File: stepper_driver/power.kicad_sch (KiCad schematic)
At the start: 3 parts

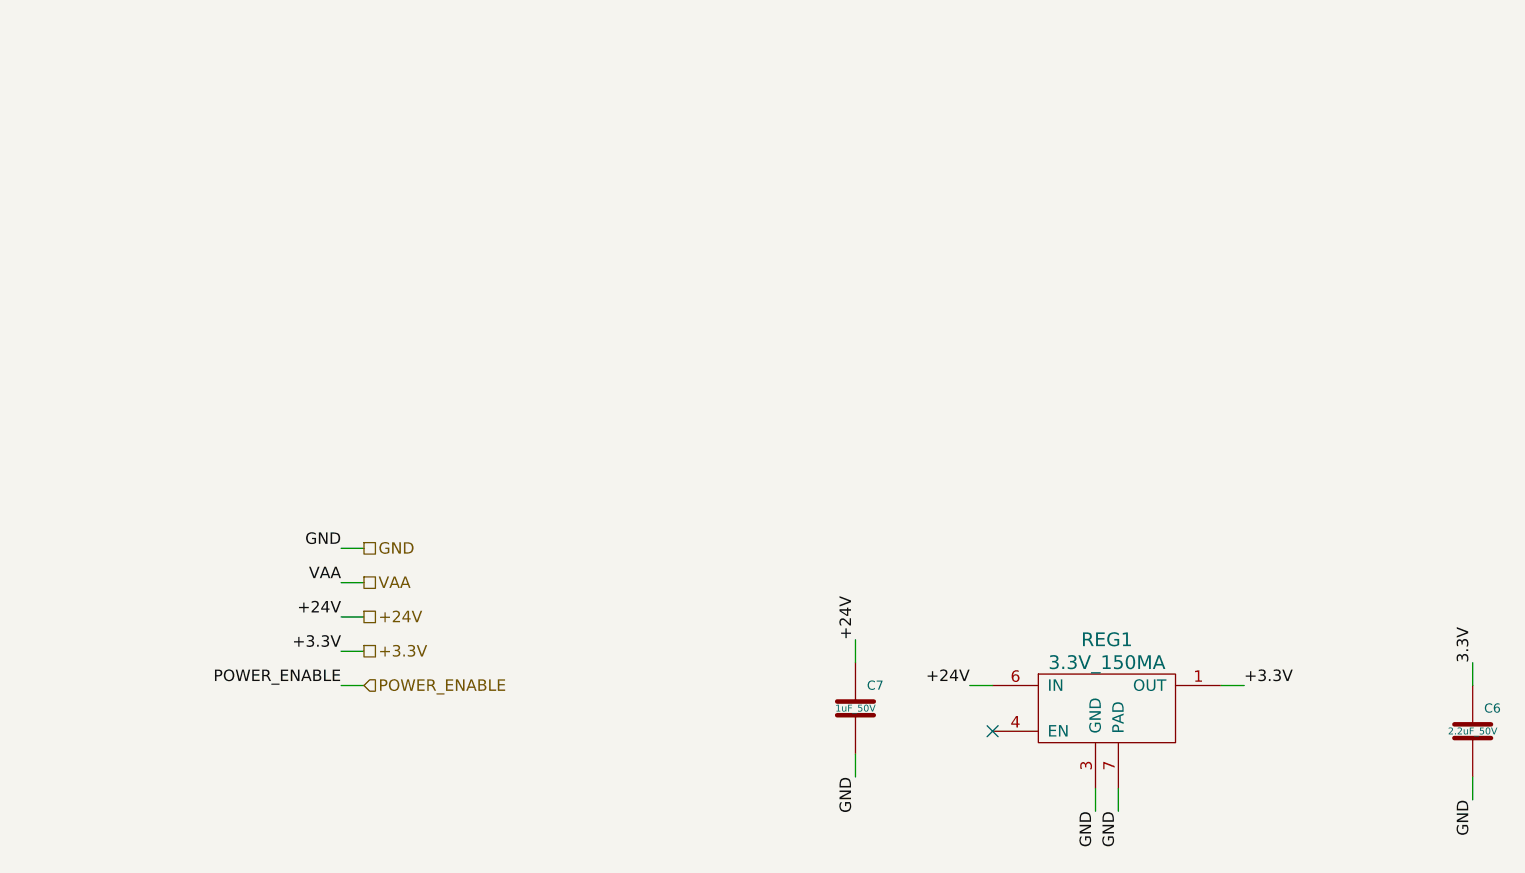
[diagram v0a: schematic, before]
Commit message: Add power enable circuitry
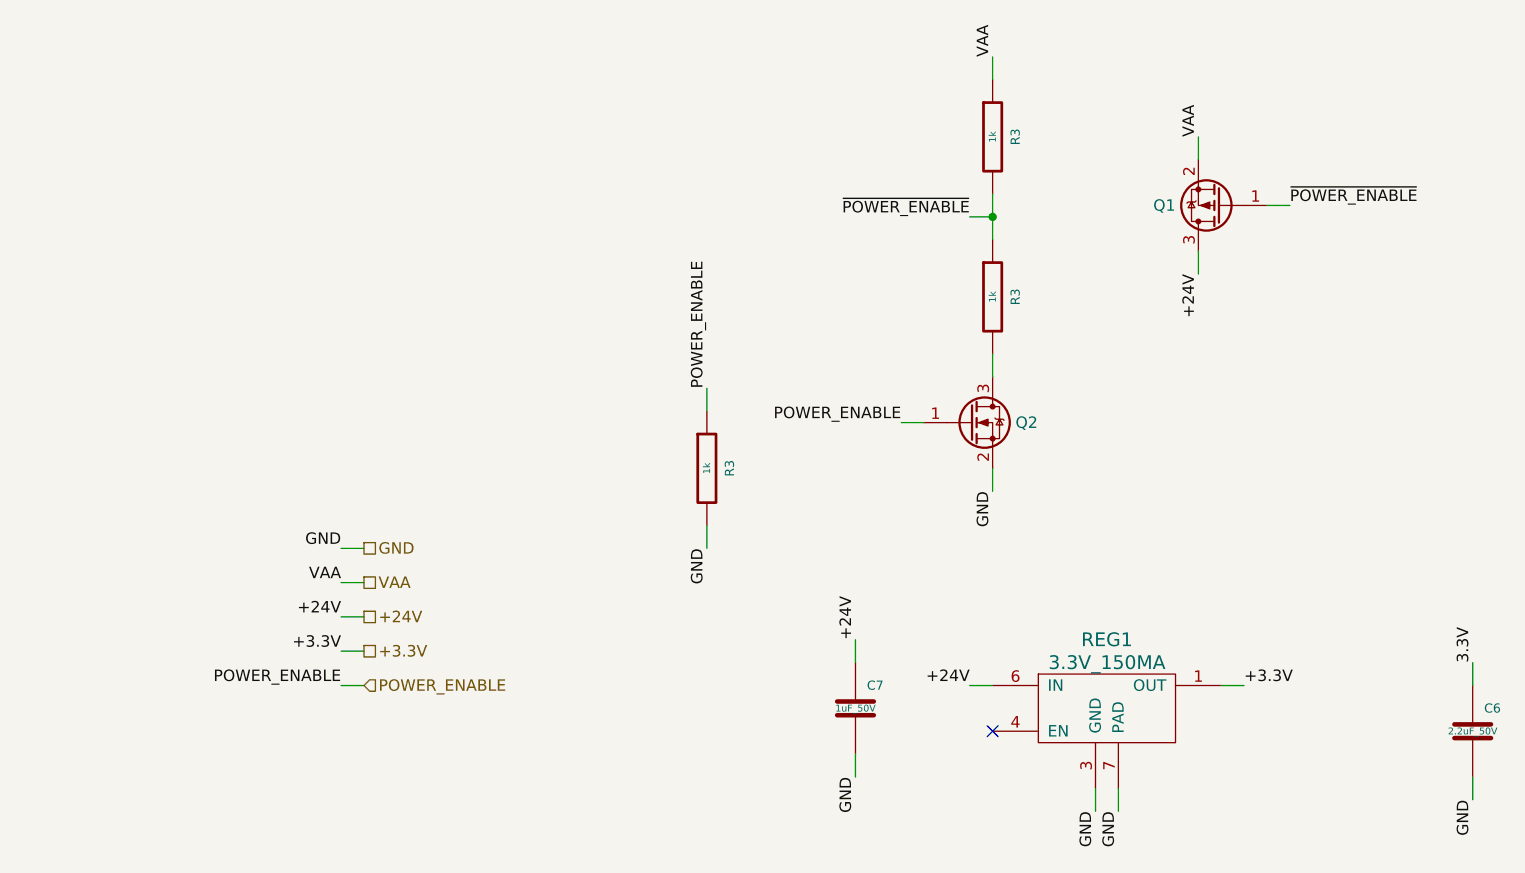
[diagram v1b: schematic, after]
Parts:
- added Q1: MOSFET-P-CH-EN-BUK6D120-60PX, Janelia:DFN2020-MD6-MOSFET, symbol Janelia:MOSFET-P-CH-EN-BUK6D120-60PX
- added Q2: MOSFET-N-CH, Janelia:XFDFN-3, symbol Janelia:MOSFET-N-CH-EN-CSD17483F4
- added R3 (x3): 1k, Janelia:R_0402_1005Metric, symbol Janelia:R_1k_0402
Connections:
- net +24V: now also Q1.3 (D)
- net GND: now also Q2.2 (S), R3.2
- net POWER_ENABLE: now also Q2.1 (G), R3.1
- net VAA: now also Q1.2 (S), R3.1
- new net: Q2.3 (D), R3.2
- new net ~{POWER_ENABLE}: Q1.1 (G), R3.1, R3.2

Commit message: Finish adding capacitors
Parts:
- renumbered Q2 to Q1, Q1 to Q2
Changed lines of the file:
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@@
   (title_block
     (title "stepper_driver")
-    (date "2023-05-05")
+    (date "2023-05-09")
     (rev "2.0")
     (company "Howard Hughes Medical Institute")
@@
         )
         (path "/cc457ebc-4af6-4663-b19f-8cb38f061cb4/4100450f-855b-4653-a714-110b9fa85f89"
-          (reference "C8") (unit 1)
+          (reference "C17") (unit 1)
         )
       )
@@
   (symbol (lib_id "Janelia:MOSFET-N-CH-EN-CSD17483F4") (at 147.32 87.63 0) (unit 1)
     (in_bom yes) (on_board yes) (dnp no) (fields_autoplaced)
-    (property "Reference" "Q2" (at 152.4 87.63 0) (do_not_autoplace)
+    (property "Reference" "Q1" (at 152.4 87.63 0) (do_not_autoplace)
       (effects (font (size 1.27 1.27)) (justify left))
     )
@@
       (project "stepper_driver"
         (path "/cc457ebc-4af6-4663-b19f-8cb38f061cb4/4100450f-855b-4653-a714-110b9fa85f89"
-          (reference "Q2") (unit 1)
+          (reference "Q1") (unit 1)
         )
       )
@@
   (symbol (lib_id "Janelia:MOSFET-P-CH-EN-BUK6D120-60PX") (at 175.26 63.5 180) (unit 1)
     (in_bom yes) (on_board yes) (dnp no)
-    (property "Reference" "Q1" (at 170.18 63.5 0)
+    (property "Reference" "Q2" (at 170.18 63.5 0)
       (effects (font (size 1.27 1.27)) (justify left))
     )
@@
       (project "stepper_driver"
         (path "/cc457ebc-4af6-4663-b19f-8cb38f061cb4/4100450f-855b-4653-a714-110b9fa85f89"
-          (reference "Q1") (unit 1)
+          (reference "Q2") (unit 1)
         )
       )
@@
         )
         (path "/cc457ebc-4af6-4663-b19f-8cb38f061cb4/4100450f-855b-4653-a714-110b9fa85f89"
-          (reference "R10") (unit 1)
+          (reference "R11") (unit 1)
         )
       )
@@
         )
         (path "/cc457ebc-4af6-4663-b19f-8cb38f061cb4/4100450f-855b-4653-a714-110b9fa85f89"
-          (reference "R11") (unit 1)
+          (reference "R10") (unit 1)
         )
       )
@@
         )
         (path "/cc457ebc-4af6-4663-b19f-8cb38f061cb4/4100450f-855b-4653-a714-110b9fa85f89"
-          (reference "C11") (unit 1)
+          (reference "C16") (unit 1)
         )
       )
@@
         )
         (path "/cc457ebc-4af6-4663-b19f-8cb38f061cb4/4100450f-855b-4653-a714-110b9fa85f89"
-          (reference "R9") (unit 1)
-        )
-      )
+          (reference "R12") (unit 1)
+        )
+      )

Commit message: Update
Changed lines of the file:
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@@
   (title_block
     (title "stepper_driver")
-    (date "2023-05-16")
+    (date "2023-05-17")
     (rev "2.0")
     (company "Howard Hughes Medical Institute")
@@
     (stroke (width 0) (type default))
   )
-  (wire (pts (xy 77.47 105.41) (xy 80.01 105.41))
+  (wire (pts (xy 62.23 88.9) (xy 59.69 88.9))
     (stroke (width 0) (type default))
   )
@@
     (stroke (width 0) (type default))
   )
-  (wire (pts (xy 77.47 116.84) (xy 80.01 116.84))
+  (wire (pts (xy 62.23 104.14) (xy 59.69 104.14))
     (stroke (width 0) (type default))
   )
@@
     (stroke (width 0) (type default))
   )
-  (wire (pts (xy 77.47 109.22) (xy 80.01 109.22))
+  (wire (pts (xy 62.23 92.71) (xy 59.69 92.71))
     (stroke (width 0) (type default))
   )
-  (wire (pts (xy 77.47 113.03) (xy 80.01 113.03))
+  (wire (pts (xy 62.23 96.52) (xy 59.69 96.52))
     (stroke (width 0) (type default))
   )
-  (wire (pts (xy 77.47 101.6) (xy 80.01 101.6))
+  (wire (pts (xy 62.23 100.33) (xy 59.69 100.33))
     (stroke (width 0) (type default))
   )
@@
     (effects (font (size 1.27 1.27)) (justify right bottom))
   )
-  (label "VAA" (at 77.47 105.41 180) (fields_autoplaced)
-    (effects (font (size 1.27 1.27)) (justify right bottom))
+  (label "VAA" (at 62.23 88.9 0) (fields_autoplaced)
+    (effects (font (size 1.27 1.27)) (justify left bottom))
   )
   (label "GND" (at 203.2 129.54 270) (fields_autoplaced)
@@
     (effects (font (size 1.27 1.27)) (justify left bottom))
   )
-  (label "+3.3V" (at 77.47 113.03 180) (fields_autoplaced)
-    (effects (font (size 1.27 1.27)) (justify right bottom))
+  (label "+3.3V" (at 62.23 96.52 0) (fields_autoplaced)
+    (effects (font (size 1.27 1.27)) (justify left bottom))
   )
   (label "~{POWER_ENABLE}" (at 147.32 64.77 180) (fields_autoplaced)
@@
     (effects (font (size 1.27 1.27)) (justify right bottom))
   )
-  (label "POWER_ENABLE" (at 77.47 116.84 180) (fields_autoplaced)
-    (effects (font (size 1.27 1.27)) (justify right bottom))
+  (label "POWER_ENABLE" (at 62.23 104.14 0) (fields_autoplaced)
+    (effects (font (size 1.27 1.27)) (justify left bottom))
   )
-  (label "GND" (at 77.47 101.6 180) (fields_autoplaced)
-    (effects (font (size 1.27 1.27)) (justify right bottom))
+  (label "GND" (at 62.23 100.33 0) (fields_autoplaced)
+    (effects (font (size 1.27 1.27)) (justify left bottom))
   )
   (label "GND" (at 134.62 127 270) (fields_autoplaced)
     (effects (font (size 1.27 1.27)) (justify right bottom))
   )
-  (label "+24V" (at 77.47 109.22 180) (fields_autoplaced)
-    (effects (font (size 1.27 1.27)) (justify right bottom))
+  (label "+24V" (at 62.23 92.71 0) (fields_autoplaced)
+    (effects (font (size 1.27 1.27)) (justify left bottom))
   )
   (label "+3.3V" (at 177.8 116.84 0) (fields_autoplaced)
     (effects (font (size 1.27 1.27)) (justify left bottom))
   )
-  (hierarchical_label "POWER_ENABLE" (shape input) (at 80.01 116.84 0) (fields_autoplaced)
-    (effects (font (size 1.27 1.27)) (justify left))
+  (hierarchical_label "POWER_ENABLE" (shape input) (at 59.69 104.14 180) (fields_autoplaced)
+    (effects (font (size 1.27 1.27)) (justify right))
   )
-  (hierarchical_label "+24V" (shape passive) (at 80.01 109.22 0) (fields_autoplaced)
-    (effects (font (size 1.27 1.27)) (justify left))
+  (hierarchical_label "+24V" (shape passive) (at 59.69 92.71 180) (fields_autoplaced)
+    (effects (font (size 1.27 1.27)) (justify right))
   )
-  (hierarchical_label "+3.3V" (shape passive) (at 80.01 113.03 0) (fields_autoplaced)
-    (effects (font (size 1.27 1.27)) (justify left))
+  (hierarchical_label "+3.3V" (shape passive) (at 59.69 96.52 180) (fields_autoplaced)
+    (effects (font (size 1.27 1.27)) (justify right))
   )
-  (hierarchical_label "VAA" (shape passive) (at 80.01 105.41 0) (fields_autoplaced)
-    (effects (font (size 1.27 1.27)) (justify left))
+  (hierarchical_label "VAA" (shape passive) (at 59.69 88.9 180) (fields_autoplaced)
+    (effects (font (size 1.27 1.27)) (justify right))
   )
-  (hierarchical_label "GND" (shape passive) (at 80.01 101.6 0) (fields_autoplaced)
-    (effects (font (size 1.27 1.27)) (justify left))
+  (hierarchical_label "GND" (shape passive) (at 59.69 100.33 180) (fields_autoplaced)
+    (effects (font (size 1.27 1.27)) (justify right))
   )
   (symbol (lib_id "Janelia:C_2.2uF_50V_0603") (at 203.2 121.92 0) (unit 1)
